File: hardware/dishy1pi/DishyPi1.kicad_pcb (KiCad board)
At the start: 4 copper layers, 87.3 x 65.3 mm, 92 parts, among them J1 GPIO, J2 TerminalBlock_2x2.54mm, J3 TerminalBlock_9x2.54mm, J4 TerminalBlock_6x2.54mm, J5 TerminalBlock_4x2.54mm, J6 TerminalBlock_9x2.54mm, J7 TerminalBlock_6x2.54mm, J8 TerminalBlock_4x2.54mm, Q1 LTV-847S, Q3 LTV-847S, Q4 LTV-847S, U1 CAT24C256WI-GT3, U2 LTC4311ISC6-TRPBF, U3 ISO1540DR, U4 LM75BIMX-5/NOPB, U5 LTV827S-TA1

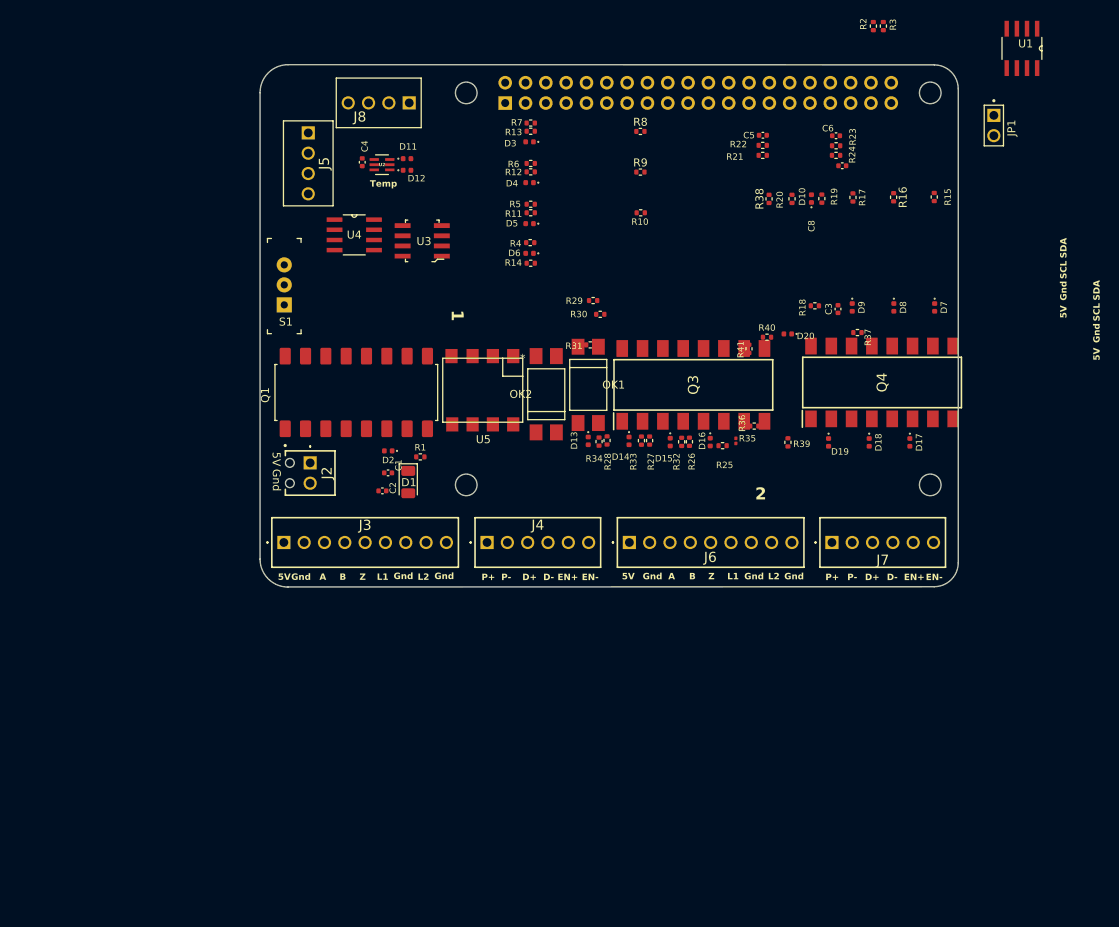
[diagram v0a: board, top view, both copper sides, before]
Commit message: Parts place in PCB layout
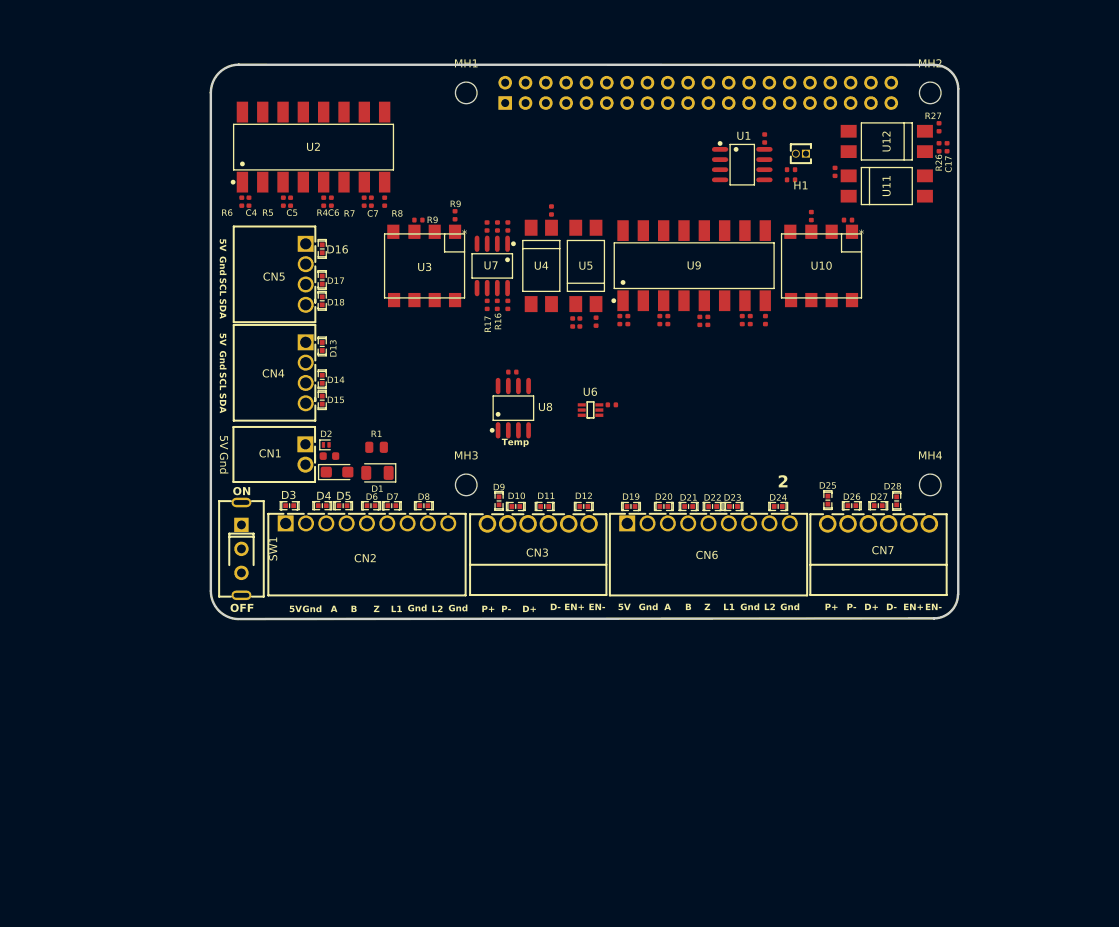
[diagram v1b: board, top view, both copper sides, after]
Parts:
- removed J2: TerminalBlock_2x2.54mm, DishFootprints:TerminalBlock_2x2.54mm
- removed J3, J6: TerminalBlock_9x2.54mm, DishFootprints:TerminalBlock_9x2.54mm
- removed J4, J7: TerminalBlock_6x2.54mm, DishFootprints:TerminalBlock_6x2.54mm
- removed J5, J8: TerminalBlock_4x2.54mm, DishFootprints:TerminalBlock_4x2.54mm
- removed JP1: JP1, DishFootprints:Header 1x2 Male
- removed OK1, OK2: LTV817S, DishFootprints:LTV817S
- removed Q1: LTV-847S, DishFootprints:LTV847S
- removed Q3, Q4: LTV-847S, DishFootprints:ACPL-847-300E
- removed R28: 10k, Resistor_SMD:R_0402_1005Metric
- removed R29, R30, R31, R39: 4R7, Resistor_SMD:R_0402_1005Metric
- removed R32, R33, R34: 470, Resistor_SMD:R_0402_1005Metric
- removed R35: 22k, Resistor_SMD:R_0201_0603Metric
- removed R36, R37, R38: 330, Resistor_SMD:R_0402_1005Metric
- removed R40: 220, Resistor_SMD:R_0402_1005Metric
- removed R41: 22k, Resistor_SMD:R_0402_1005Metric
- removed S1: EG1218, digikey-footprints:Switch_Slide_11.6x4mm_EG1218
- added C10: 100nF, PCM_JLCPCB:C_0402, F.Cu at (108.7, 64.2)
- added C11: 100nF, PCM_JLCPCB:C_0402, F.Cu at (108.7, 74.0)
- added C12: 100nF, PCM_JLCPCB:C_0402, F.Cu at (109.3, 82.4)
- added C13: 100pF, PCM_JLCPCB:C_0402, F.Cu at (123.7, 75.9)
- added C14: 100pF, PCM_JLCPCB:C_0402, F.Cu at (127.7, 75.9)
- added C15: 100pF, PCM_JLCPCB:C_0402, F.Cu at (133.7, 76.0)
- added C16: 100pF, PCM_JLCPCB:C_0402, F.Cu at (139.0, 75.9)
- added C17: 100pF, PCM_JLCPCB:C_0402, F.Cu at (163.6, 54.3)
- added C7: 100pF, PCM_JLCPCB:C_0402, F.Cu at (91.6, 61.1)
- added C9: 100nF, PCM_JLCPCB:C_0402, F.Cu at (121.7, 86.5)
- added CN1: KF2EDGR-2.54-2P, MyParts:CONN-TH_P2.54_KF2EDGR-2.54-2P, F.Cu at (83.4, 92.7)
- added CN2: KF2EDGR-2.54-9P, MyParts:CONN-TH_9P-P2.54_KF2EDGR-2.54-9P, F.Cu at (91.1, 101.3)
- added CN3: KF2EDGR-2.54-6P, MyParts:CONN-TH_KF2EDGR-2.54-6P, F.Cu at (112.5, 101.4)
- added CN4: KF2EDGR-2.54-4P, MyParts:CONN-TH_4P-P2.54_KF2EDGR-2.54-4P, F.Cu at (83.4, 82.5)
- added CN5: KF2EDGR-2.54-4P, MyParts:CONN-TH_4P-P2.54_KF2EDGR-2.54-4P, F.Cu at (83.4, 70.2)
- added CN6: KF2EDGR-2.54-9P, MyParts:CONN-TH_9P-P2.54_KF2EDGR-2.54-9P, F.Cu at (133.8, 101.3)
- added CN7: KF2EDGR-2.54-6P, MyParts:CONN-TH_KF2EDGR-2.54-6P, F.Cu at (155.0, 101.4)
- added D21: TPESD0402G05V, MyParts:D0402-BI, F.Cu at (131.3, 99.2)
- added D22: TPESD0402G05V, MyParts:D0402-BI, F.Cu at (134.3, 99.2)
- added D23: TPESD0402G05V, MyParts:D0402-BI, F.Cu at (136.9, 99.2)
- added D24: TPESD0402G05V, MyParts:D0402-BI, F.Cu at (142.5, 99.2)
- added D25: TPESD0402G05V, MyParts:D0402-BI, F.Cu at (148.7, 98.4)
- added D26: TPESD0402G05V, MyParts:D0402-BI, F.Cu at (151.7, 99.1)
- added D27: TPESD0402G05V, MyParts:D0402-BI, F.Cu at (155.0, 99.1)
- added D28: TPESD0402G05V, MyParts:D0402-BI, F.Cu at (157.3, 98.5)
- added H1: 1.27MM/1*2P, MyParts:HDR-TH_2P-P1.27-V-M, F.Cu at (145.3, 55.1)
- added SW1: SS-12F49-G050, MyParts:SW-TH_SS-12F45-GXXX, F.Cu at (75.4, 104.5)
- added U10: LTV-827S-TA1, MyParts:LTV827S-TA1, F.Cu at (147.9, 69.1)
- added U11: LTV-817S-TA1, MyParts:LTV817S, F.Cu at (156.1, 59.1)
- added U12: LTV-817S-TA1, MyParts:LTV817S, F.Cu at (156.1, 53.6)
- added U6: LTC4311ISC6#TRPBF, MyParts:SC-70-6_L2.2-W1.3-P0.65-LS2.2-BL, F.Cu at (119.0, 87.2)
- added U7: ISO1540DR, MyParts:SOIC-8_L4.9-W3.9-P1.27-LS6.0-BL, F.Cu at (106.8, 69.1)
- added U8: LM75BIMX-5/NOPB, MyParts:SOIC-8_L4.9-W3.9-P1.27-LS6.0-BL, F.Cu at (109.4, 86.9)
- added U9: LTV-847S, MyParts:SMD-16_L20.0-W6.5-P2.54-LS10.2-BL, F.Cu at (132.0, 69.1)
- C1: value 0.1uF -> 100nF; footprint Capacitor_SMD:C_0402_1005Metric -> PCM_JLCPCB:C_0603
- C2: footprint Capacitor_SMD:C_0402_1005Metric -> PCM_JLCPCB:C_CASE-A-3216-18(mm)
- C3: value 100n -> 100nF; footprint Capacitor_SMD:C_0402_1005Metric -> PCM_JLCPCB:C_0402
- C4, C5, C6, C8: value 0.1uF -> 100pF; footprint Capacitor_SMD:C_0402_1005Metric -> PCM_JLCPCB:C_0402
- D10, D11, D12, D13, D14, D15, D16, D17, D18, D19, D20, D3, D4, D5, D6, D7, D8, D9: footprint Diode_SMD:D_0402_1005Metric -> MyParts:D0402-BI
- D2: footprint Diode_SMD:D_0402_1005Metric -> Diode_SMD:D_SOD-882
- R1: value 1k -> 1kΩ; footprint Resistor_SMD:R_0402_1005Metric -> PCM_JLCPCB:R_0805
- R11: value 470 -> 1kΩ; footprint Resistor_SMD:R_0402_1005Metric -> PCM_JLCPCB:R_0402
- R12: value 470 -> 470Ω; footprint Resistor_SMD:R_0402_1005Metric -> PCM_JLCPCB:R_0402
- R13: value 470 -> 22kΩ; footprint Resistor_SMD:R_0402_1005Metric -> PCM_JLCPCB:R_0402
- R14: value 22k -> 4.7kΩ; footprint Resistor_SMD:R_0402_1005Metric -> PCM_JLCPCB:R_0402
- R15, R16, R17: value 330 -> 4.7kΩ; footprint Resistor_SMD:R_0402_1005Metric -> PCM_JLCPCB:R_0402
- R18, R23, R24, R9: value 4R7 -> 1kΩ; footprint Resistor_SMD:R_0402_1005Metric -> PCM_JLCPCB:R_0402
- R19, R25, R4: value 220 -> 1kΩ; footprint Resistor_SMD:R_0402_1005Metric -> PCM_JLCPCB:R_0402
- R2, R3: value 3.9k -> 3.9kΩ; footprint Resistor_SMD:R_0402_1005Metric -> PCM_JLCPCB:R_0402
- R20: value 22k -> 1kΩ; footprint Resistor_SMD:R_0402_1005Metric -> PCM_JLCPCB:R_0402
- R21: value 4R7 -> 220Ω; footprint Resistor_SMD:R_0402_1005Metric -> PCM_JLCPCB:R_0402
- R22, R8: value 4R7 -> 22kΩ; footprint Resistor_SMD:R_0402_1005Metric -> PCM_JLCPCB:R_0402
- R26: value 10k -> 470Ω; footprint Resistor_SMD:R_0402_1005Metric -> PCM_JLCPCB:R_0402
- R27: value 10k -> 22kΩ; footprint Resistor_SMD:R_0402_1005Metric -> PCM_JLCPCB:R_0402
- R5, R6: value 10k -> 1kΩ; footprint Resistor_SMD:R_0402_1005Metric -> PCM_JLCPCB:R_0402
- R7: value 10k -> 220Ω; footprint Resistor_SMD:R_0402_1005Metric -> PCM_JLCPCB:R_0402
- R9: renamed from R10; value 4R7 -> 1kΩ; footprint Resistor_SMD:R_0402_1005Metric -> PCM_JLCPCB:R_0402
- U1: footprint DishFootprints:CAT24C256_EEPROM -> MyParts:SOIC-8_L4.9-W3.9-P1.27-LS6.0-BL
- U2: value LTC4311ISC6-TRPBF -> LTV-847S; footprint DishFootprints:LTC4311 -> MyParts:SMD-16_L20.0-W6.5-P2.54-LS10.2-BL
- U3: value ISO1540DR -> LTV-827S-TA1; footprint digikey-footprints:SOIC-8_W3.9mm -> MyParts:LTV827S-TA1
- U4: value LM75BIMX-5/NOPB -> LTV-817S-TA1; footprint DishFootprints:M08A -> MyParts:LTV817S
- U5: value LTV827S-TA1 -> LTV-817S-TA1; footprint DishFootprints:LTV827S -> MyParts:LTV817S
- moved D17 76.2 mm to (85.5, 70.9)
- moved D7 72.2 mm to (94.2, 99.1), turned to 0 degrees
- moved D18 70.6 mm to (85.5, 73.5)
- moved D8 63.8 mm to (98.2, 99.1), turned to 180 degrees
- moved C6 63.6 mm to (86.6, 61.1), turned to 90 degrees
- moved C5 59.6 mm to (81.5, 61.1), turned to 90 degrees
- moved R15 54.7 mm to (107.4, 64.2)
- moved D3 54.5 mm to (81.4, 99.1), turned to 0 degrees
- moved D16 54.2 mm to (85.5, 67.0), turned to 90 degrees
- moved D10 53.4 mm to (109.7, 99.2), turned to 0 degrees
- moved R27 53.3 mm to (162.6, 51.8)
- moved R16 51.3 mm to (107.4, 74.0)
- moved D9 50.3 mm to (107.6, 98.5), turned to 90 degrees
- moved R26 48.3 mm to (162.6, 54.3), turned to -90 degrees
- moved D4 48.0 mm to (85.5, 99.1)
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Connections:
- C4 pad 1: +5V -> GNDIO
- C4 pad 2: GNDIO -> Net-(U2-AN1)
- C5 pad 1: +3.3V -> GNDIO
- C5 pad 2: GNDPI -> Net-(U2-AN2)
- C6 pad 1: +5V -> GNDIO
- C6 pad 2: GNDIO -> Net-(U2-AN3)
- C8 pad 1: GNDIO -> Net-(C8-Pad1)
- C8 pad 2: +5V -> GNDIO
- D10 pad 1: Net-(D10-K) -> /IO/PUL-
- D10 pad 2: /IO/LIM_2 -> GNDIO
- D11 pad 1: /I2C/SDA -> /IO/DIR-
- D12 pad 1: /I2C/SCL -> /IO/MF-
- D13 pad 1: Net-(D13-K) -> +5V
- D14 pad 1: Net-(D14-K) -> /I2C/SCL
- D15 pad 1: Net-(D15-K) -> /I2C/SDA
- D16 pad 1: Net-(D16-K) -> GNDIO
- D16 pad 2: /io2/LIM_1 -> +5V
- D17 pad 1: /io2/PUL- -> GNDIO
- D17 pad 2: GNDIO -> /I2C/SCL
- D18 pad 1: /io2/DIR- -> GNDIO
- D18 pad 2: GNDIO -> /I2C/SDA
- D19 pad 1: /io2/MF- -> +5V
- D20 pad 1: Net-(D20-K) -> /io2/ENC_A
- D20 pad 2: /io2/LIM_2 -> GNDIO
- D3 pad 1: Net-(D3-K) -> +5V
- D4 pad 1: Net-(D4-K) -> /IO/ENC_A
- D5 pad 1: Net-(D5-K) -> /IO/ENC_B
- D6 pad 1: Net-(D6-K) -> /IO/ENC_Z
- D6 pad 2: /IO/LIM_1 -> GNDIO
- D7 pad 1: /IO/PUL- -> /IO/LIM_1
- D8 pad 1: /IO/DIR- -> /IO/LIM_2
- D9 pad 1: /IO/MF- -> +5V
- R11 pad 1: Net-(D5-K) -> E_MF/24
- R11 pad 2: /IO/ENC_Z -> Net-(R11-Pad2)
- R12 pad 1: Net-(D4-K) -> +5V
- R12 pad 2: /IO/ENC_B -> Net-(C8-Pad1)
- R13 pad 1: Net-(D3-K) -> /IO/LIM_2
- R13 pad 2: /IO/ENC_A -> GNDIO
- R14 pad 1: GNDIO -> +3.3V
- R14 pad 2: /IO/LIM_1 -> PI_SCL
- R15 pad 1: E_PUL/18 -> +3.3V
- R15 pad 2: Net-(R15-Pad2) -> PI_SDA
- R16 pad 1: E_DIR/23 -> +5V
- R16 pad 2: Net-(R16-Pad2) -> /I2C/SDA
- R17 pad 1: E_MF/24 -> +5V
- R17 pad 2: Net-(OK1-Pad1) -> /I2C/SCL
- R18 pad 1: +3.3V -> /io2/ENC_Z
- R18 pad 2: E_LIM_2/16 -> Net-(U9-AN3)
- R19 pad 1: +5V -> /io2/ENC_B
- R19 pad 2: Net-(D10-K) -> Net-(U9-AN2)
- R2 pad 2: /ID_SDA -> /ID_SCL
- R20 pad 1: GNDIO -> /io2/ENC_A
- R20 pad 2: /IO/LIM_2 -> Net-(U9-AN1)
- R21 pad 1: +3.3V -> +5V
- R21 pad 2: PI_SCL -> Net-(U9-AN4)
- R22 pad 1: +3.3V -> /io2/LIM_1
- R22 pad 2: PI_SDA -> GNDIO
- R23 pad 1: +5V -> A_PUL/13
- R23 pad 2: /I2C/SDA -> Net-(R23-Pad2)
- R24 pad 1: +5V -> A_DIR/19
- R24 pad 2: /I2C/SCL -> Net-(R24-Pad2)
- R25 pad 1: Net-(D16-K) -> A_MF/20
- R25 pad 2: +5V -> Net-(R25-Pad2)
- R26 pad 1: /io2/ENC_Z -> +5V
- R26 pad 2: +5V -> Net-(C17-Pad1)
- R27 pad 1: /io2/ENC_B -> /io2/LIM_2
- R27 pad 2: +5V -> GNDIO
- R3 pad 2: /ID_SCL -> /ID_SDA
- R4 pad 1: Net-(D6-K) -> /IO/ENC_Z
- R4 pad 2: +5V -> Net-(U2-AN3)
- R5 pad 1: /IO/ENC_Z -> /IO/ENC_B
- R5 pad 2: +5V -> Net-(U2-AN2)
- R6 pad 1: /IO/ENC_B -> /IO/ENC_A
- R6 pad 2: +5V -> Net-(U2-AN1)
- R7 pad 1: /IO/ENC_A -> +5V
- R7 pad 2: +5V -> Net-(U2-AN4)
- R8 pad 1: E_ENC_A/17 -> /IO/LIM_1
- R8 pad 2: +3.3V -> GNDIO
- R9 pad 1: E_ENC_Z/27 -> E_DIR/23
- R9 pad 2: +3.3V -> Net-(R10-Pad2)
- R9 pad 1: E_ENC_B/22 -> E_PUL/18
- R9 pad 2: +3.3V -> Net-(R9-Pad2)
- U2 pad 1: +5V -> Net-(U2-AN1)
- U2 pad 3: +5V -> Net-(U2-AN2)
- U2 pad 4: /I2C/SCL -> GNDIO
- U2 pad 5: GNDIO -> Net-(U2-AN3)
- U2 pad 6: /I2C/SDA -> GNDIO
- U3 pad 1: +3.3V -> Net-(R9-Pad2)
- U3 pad 2: PI_SDA -> GNDPI
- U3 pad 3: PI_SCL -> Net-(R10-Pad2)
- U3 pad 6: /I2C/SCL -> /IO/DIR-
- U3 pad 7: /I2C/SDA -> GNDIO
- U3 pad 8: +5V -> /IO/PUL-
- U4 pad 1: /I2C/SDA -> Net-(R11-Pad2)
- U4 pad 2: /I2C/SCL -> GNDPI
- U4 pad 3: unconnected-(U4-O.S.-Pad3) -> GNDIO
- U4 pad 4: GNDIO -> /IO/MF-
- U5 pad 1: Net-(R15-Pad2) -> Net-(C8-Pad1)
- U5 pad 2: GNDPI -> /IO/LIM_2
- U5 pad 3: Net-(R16-Pad2) -> GNDPI
- U5 pad 4: GNDPI -> E_LIM_2/16
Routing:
- added copper zone on In1.Cu, net GNDIO
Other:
- board size 87.3 x 65.3 mm -> 93.4 x 69.3 mm
- board text added: "OFF"
- board text added: "ON"
- board text added: "U8"
- board text removed: "1"

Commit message: Ground and Power planes placed
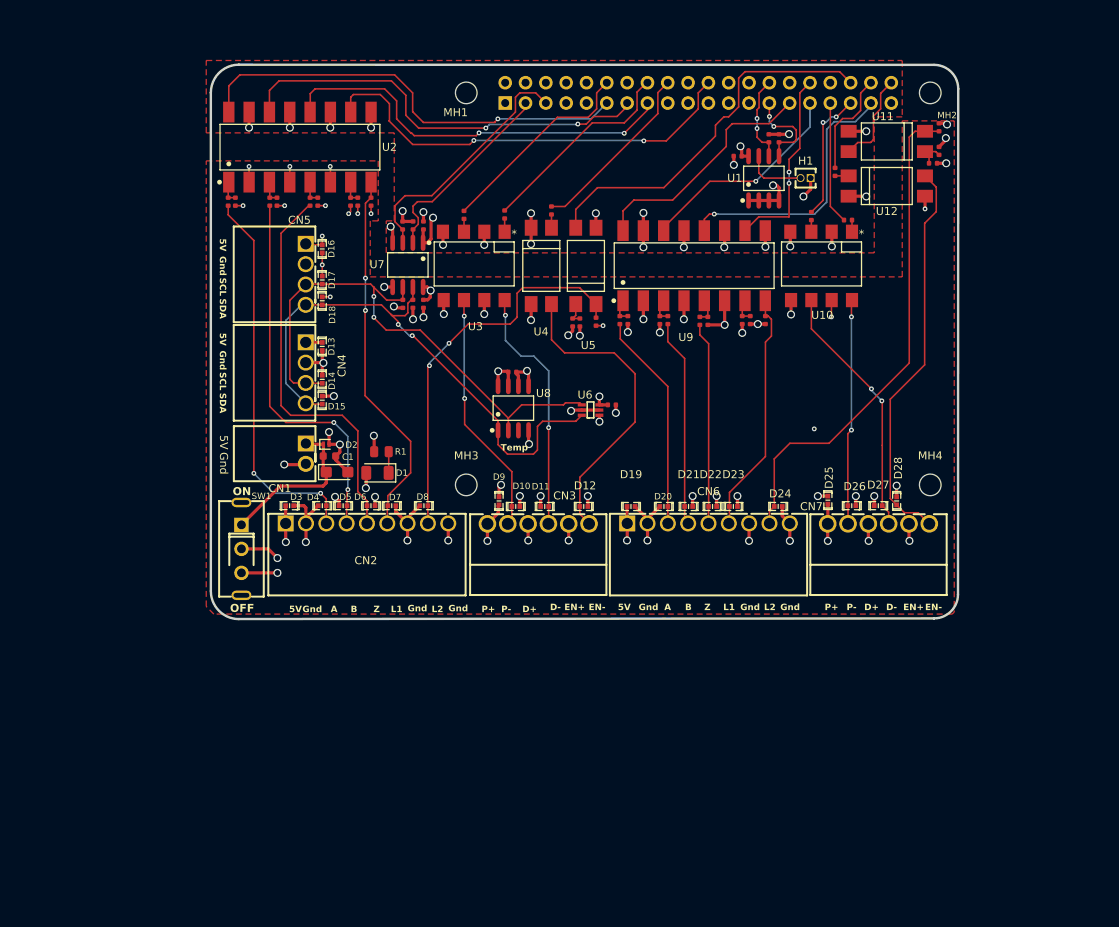
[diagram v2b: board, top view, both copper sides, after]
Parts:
- removed the R9 at (97.5, 63.4)
- removed the R9 at (102.1, 62.8)
- added R10: 1kΩ, PCM_JLCPCB:R_0402, F.Cu at (108.3, 62.7)
- added R9: 1kΩ, PCM_JLCPCB:R_0402, F.Cu at (103.2, 62.8)
- D2: value TPESD0402G05V -> PESD5V0L1UL
- J1: value GPIO -> Conn_02x20_Odd_Even
- moved C10 10.6 mm to (98.1, 64.1)
- moved C11 10.6 mm to (98.1, 73.9)
- moved R15 10.6 mm to (96.8, 64.1)
- moved R16 10.6 mm to (96.8, 73.9), turned to 90 degrees
- moved R17 10.6 mm to (95.6, 73.9)
- moved U7 10.6 mm to (96.2, 69.0)
- moved R14 10.6 mm to (95.5, 64.1)
- moved U3 6.20 mm to (104.5, 69.1)
- moved R3 5.40 mm to (142.6, 53.2), turned to -90 degrees
- moved R2 4.80 mm to (141.3, 53.2), turned to -90 degrees
- moved C3 4.03 mm to (137.4, 55.4), turned to 180 degrees
- moved U1 3.19 mm to (140.7, 58.2), turned to 0 degrees
- moved H1 3.11 mm to (145.9, 58.1)
- moved C17 2.66 mm to (161.8, 56.3), turned to 0 degrees
- moved C4 1.70 mm to (74.6, 61.1)
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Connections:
- U3 pad 6: /IO/DIR- -> /IO/PUL-
- U3 pad 8: /IO/PUL- -> /IO/DIR-
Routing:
- net GNDIO: track 0.00 -> 131.2 mm, vias 0 -> 59
- net /I2C/SDA: track 0.00 -> 70.6 mm, vias 0 -> 2
- net /I2C/SCL: track 0.00 -> 69.0 mm, vias 0 -> 2
- net /io2/LIM_2: track 0.00 -> 62.4 mm
- net +5V: track 0.00 -> 57.5 mm, vias 0 -> 21
- net E_ENC_A/17: track 0.00 -> 56.0 mm, vias 0 -> 1
- net E_LIM_1/25: track 0.00 -> 55.0 mm, vias 0 -> 2
- net E_ENC_B/22: track 0.00 -> 53.4 mm, vias 0 -> 2
- net E_ENC_Z/27: track 0.00 -> 51.1 mm, vias 0 -> 2
- net /IO/ENC_Z: track 0.00 -> 49.7 mm
- net /io2/MF-: track 0.00 -> 49.5 mm
- net /IO/LIM_2: track 0.00 -> 49.2 mm, vias 0 -> 2
- net /IO/ENC_A: track 0.00 -> 48.2 mm, vias 0 -> 2
- net /IO/ENC_B: track 0.00 -> 47.4 mm, vias 0 -> 2
- net E_LIM_2/16: track 0.00 -> 47.3 mm
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- added copper zone on In2.Cu, net +3.3V
- added copper zone on In2.Cu, net +5V
- added copper zone on F.Cu, net GNDIO
- added copper zone on F.Cu, net GNDPI
- added copper zone on In1.Cu, net GNDPI
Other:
- outline, holes or cut-outs redrawn
- board text removed: "2"

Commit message: Modifications based on first board assembly
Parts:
- added G***: LOGO, LOGO, F.Cu at (147.2, 83.2)
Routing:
- net GNDPI: vias 22 -> 101
- net GNDIO: vias 59 -> 196
- added copper zone on B.Cu, net GNDIO
- added copper zone on B.Cu, net GNDPI
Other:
- board text added: "Axis 1"
- board text added: "Axis 2"
- board text added: "Control 2 Axis Encoder Input/Motor Controller Pulse Dir Output I2C for external sensors"
- board text added: "DishyPi1 Raspberry Pi Hat"
- board text added: "Version 1.0"
- board text added: "www.jrdish.com"
